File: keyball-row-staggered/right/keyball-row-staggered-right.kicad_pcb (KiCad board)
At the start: 2 copper layers, 178.2 x 113.8 mm, 91 parts, among them J11 trackball, J12 MJ-4PP-9, SW1 SW_PUSH, SW10 SW_PUSH, SW11 SW_PUSH, SW12 SW_PUSH, SW13 SW_PUSH, SW14 SW_PUSH, SW15 SW_PUSH, SW16 SW_PUSH, SW17 SW_PUSH, SW18 SW_PUSH, SW19 SW_PUSH, SW2 SW_PUSH, SW20 SW_PUSH, SW21 SW_PUSH, SW22 SW_PUSH, SW23 SW_PUSH, SW24 SW_PUSH, SW25 SW_PUSH, SW26 SW_PUSH, SW27 SW_PUSH, SW28 SW_PUSH, SW29 SW_PUSH, SW3 SW_PUSH, SW30 SW_PUSH, SW31 SW_PUSH, SW32 SW_PUSH, SW33 SW_PUSH, SW34 SW_PUSH, SW4 SW_PUSH, SW5 SW_PUSH, SW6 SW_PUSH, SW7 SW_PUSH, SW8 SW_PUSH, SW9 SW_PUSH, U1 ProMicro

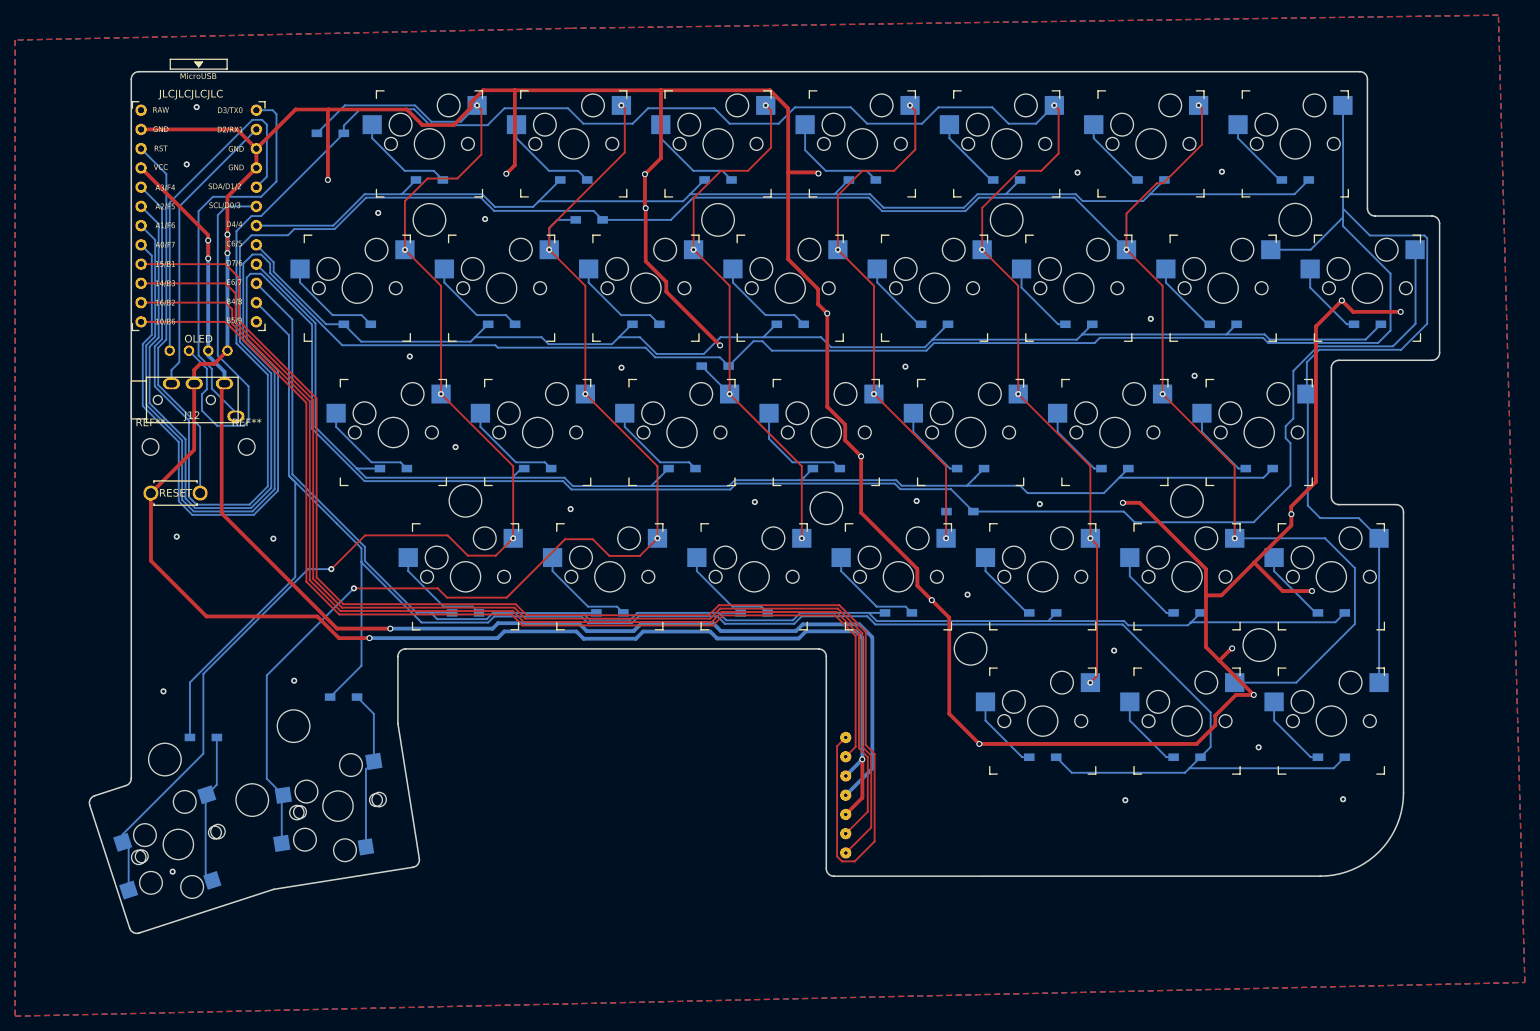
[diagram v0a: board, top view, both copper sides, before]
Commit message: キーボード側をtrackball基板に合わせて修正
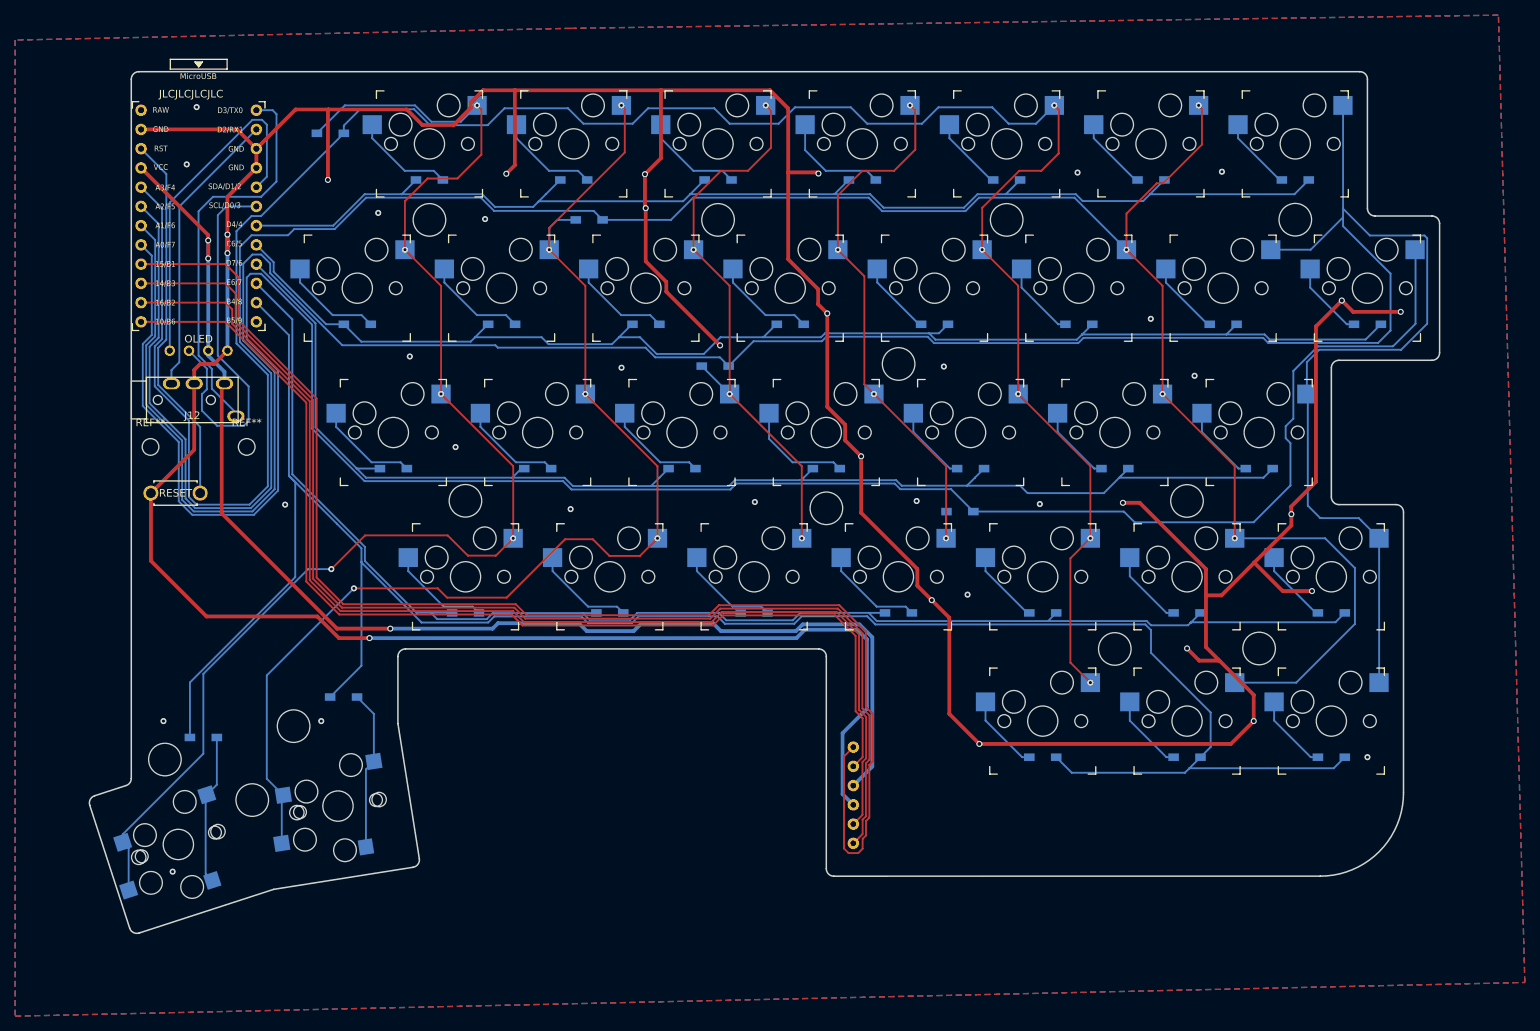
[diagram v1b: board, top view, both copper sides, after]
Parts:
- removed J11: trackball, tsuburin-keyboard:keyball_trackball
- added J1: trackball-header-master, tsuburin-keyboard:keyball_trackball_header_master, F.Cu at (141.9, 133.6)
- added Ref**: Val**, kbd:spacer_m2, F.Cu at (147.7, 76.7)
- moved Ref** 19.0 mm to (176.2, 114.3)
- moved Ref** 0.45 mm to (195.2, 114.2)
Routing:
- net SCLK: track 184.7 -> 180.5 mm
- net MOSI: track 157.0 -> 155.1 mm
- net MISO: track 162.4 -> 160.5 mm
- net ROW4: track 271.2 -> 273.0 mm
- net VCC: track 169.9 -> 168.2 mm
- net NCS: track 142.9 -> 144.6 mm
- net COL0: track 304.7 -> 306.1 mm
- net GND: track 583.1 -> 582.7 mm, vias 47 -> 42

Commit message: nenecchi追加
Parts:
- added G***: LOGO, tsuburin-keyboard:nenecchi-qmk-kanzenrikai, F.Cu at (178.4, 137.8)
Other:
- board text removed: "JLCJLCJLCJLC"
